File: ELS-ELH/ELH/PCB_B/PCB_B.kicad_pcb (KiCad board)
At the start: 2 copper layers, 95 x 95 mm, 22 parts, among them J1 Pressure Transducer Input, J2 Conn_01x04_Pin, J3 Conn_01x20_Pin, J4 Conn_01x20_Pin, U1 GY-87

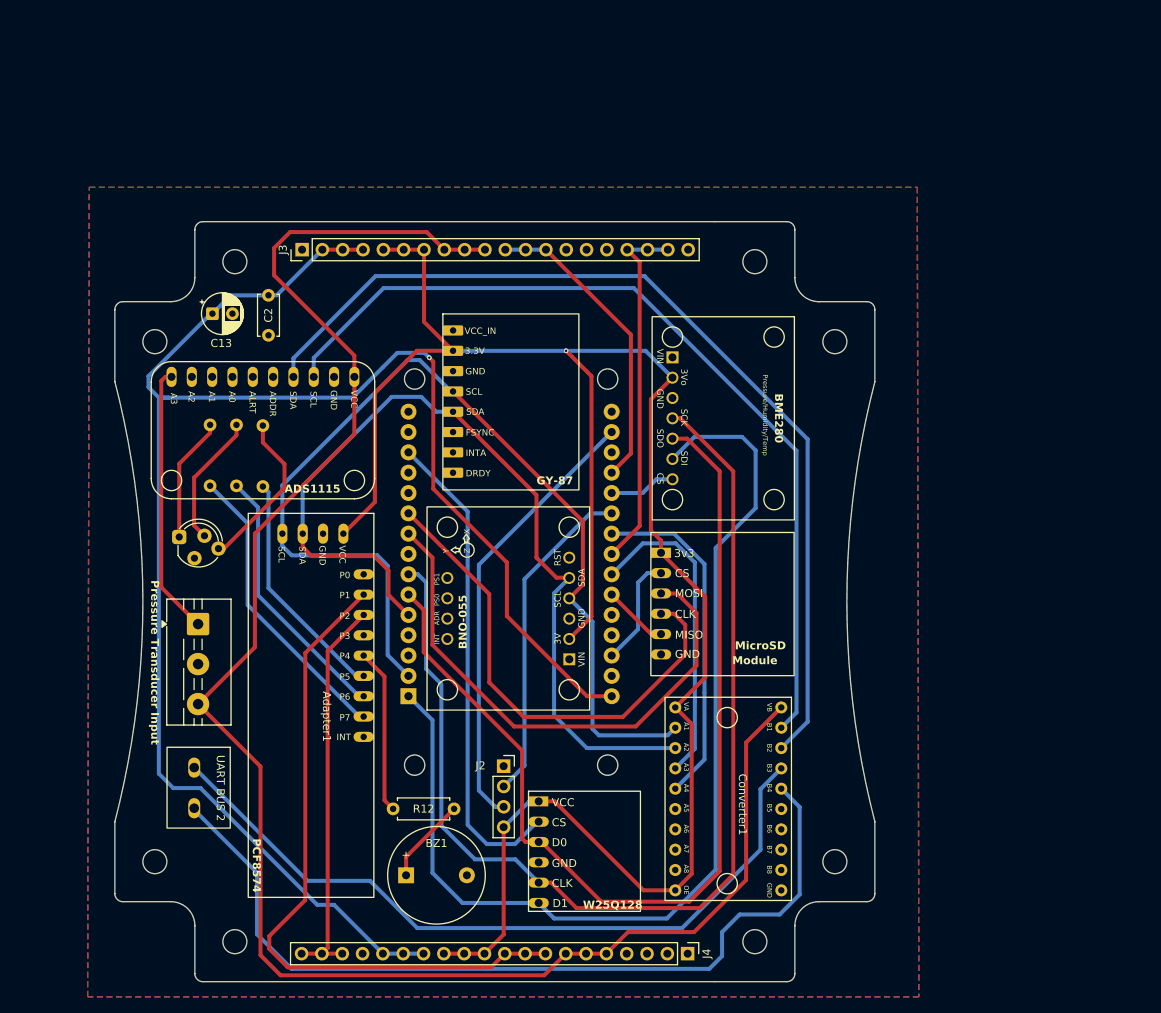
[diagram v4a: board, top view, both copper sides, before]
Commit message: General Update
Final version & manufacture files of both PCBs + codes of unit testing on modules and functionalities

* Update on net labels of both PCBs

* Update in symbols and footprints

* Unitary Tests Codes

* Update on schematics B

* Update in PCB B - new layout

* Update in schematic A

* PCB B Almost finishhed

* PCB B ready, PCB A layout ready

* Finish PCB B

* Solve DRC problems with B

* PCB A routed

* reorganized resistances

* regulator's names changed

* Update almost finished

* Finished the manufacture

---------

Co-authored-by: sofiamelo02 <sofia.melo@udea.edu.co>
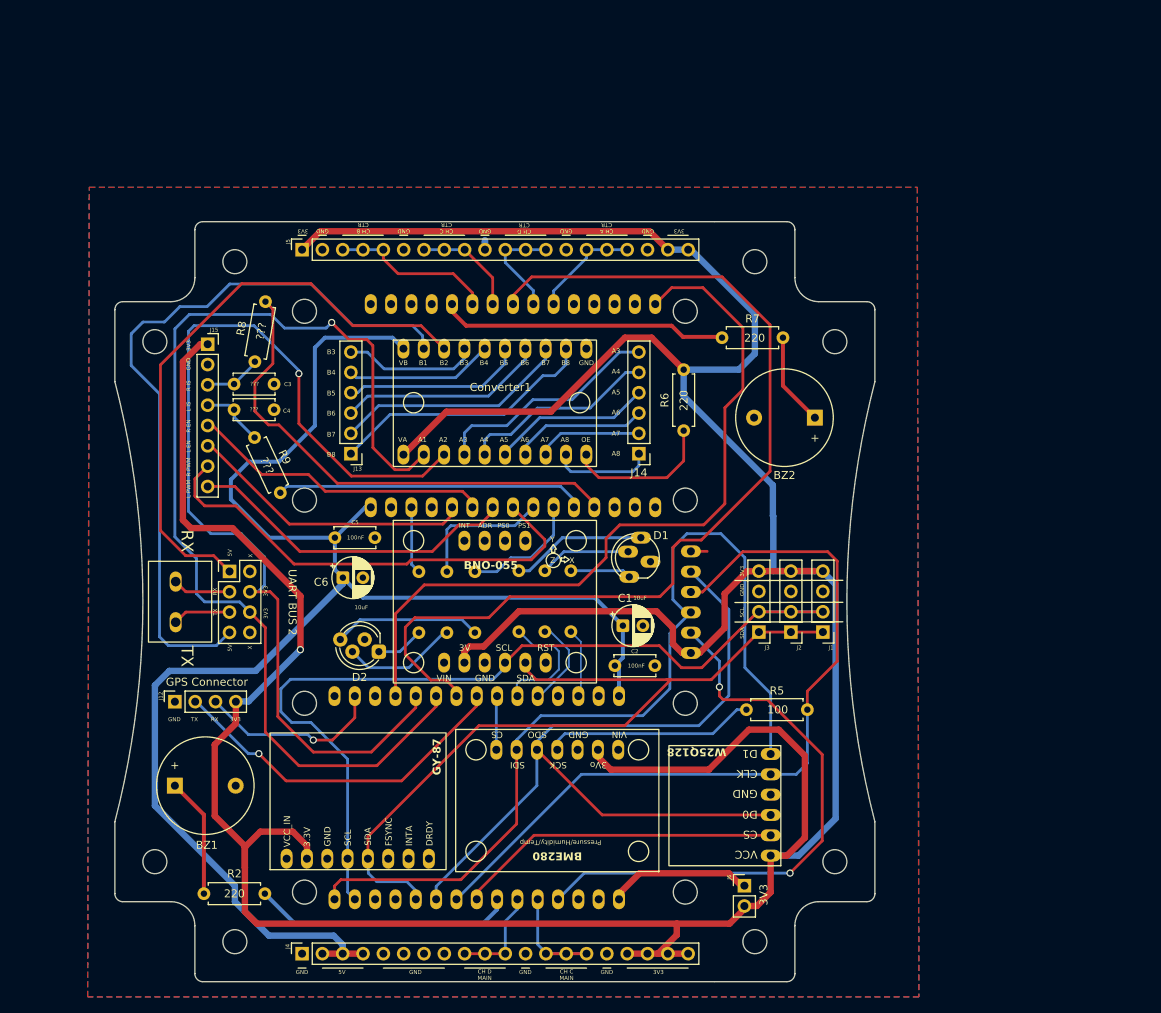
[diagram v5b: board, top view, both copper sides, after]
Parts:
- removed ADC1: ADS1115, ELH_Library:ADS1115
- removed Adapter1: PCF8574, ELH_Library:PCF8574
- removed BME2: BME280, ELH_Library:BME280
- removed Bornera7: UART BUS 2, ELH_Library:Bornera 2P
- removed C13: 10uF, Capacitor_THT:CP_Radial_D5.0mm_P2.50mm
- removed D10: LED_RKGB, ELH_Library:LED RGB
- removed ESP1: ESP32 DEVKIT V1, ELH_Library:ESP32 DEVKIT V1
- removed IMU3: BNO055, ELH_Library:BNO055
- added BME1: BME280, ELH_Library:BME280, F.Cu at (20.5, 33.8)
- added BZ2: Buzzer, Buzzer_Beeper:Buzzer_12x9.5RM7.6, F.Cu at (40.0, -23.0)
- added Bornera1: UART BUS 2, ELH_Library:Bornera 2P, F.Cu at (-35.4, -5.05)
- added C1: 10uF, Capacitor_THT:CP_Radial_D5.0mm_P2.50mm, F.Cu at (16.0, 3.00)
- added C3: ???, Capacitor_THT:C_Disc_D5.0mm_W2.5mm_P5.00mm, F.Cu at (-27.6, -27.2)
- added C4: ???, Capacitor_THT:C_Disc_D5.0mm_W2.5mm_P5.00mm, F.Cu at (-32.6, -24.0)
- added C5: 100nF, Capacitor_THT:C_Disc_D5.0mm_W2.5mm_P5.00mm, F.Cu at (-15.0, -8.00)
- added C6: 10uF, Capacitor_THT:CP_Radial_D5.0mm_P2.50mm, F.Cu at (-19.0, -3.00)
- added D1: LED_RKGB, ELH_Library:LED RGB, F.Cu at (17.1, -5.00)
- added D2: LED_RKGB, LED_THT:LED_D5.0mm-4_RGB_Staggered_Pins, F.Cu at (-14.5, 6.25)
- added ESP_CTR1: ESP32 DEVKIT V1, ELH_Library:ESP32 DEVKIT V1, B.Cu at (0.00, -25.0)
- added ESP_MAIN1: ESP32 DEVKIT V1, ELH_Library:ESP32 DEVKIT V1, B.Cu at (0.00, 25.0)
- added G***: LOGO, ELH_Library:deltav_logo, B.Cu at (32.9, -18.5)
- added G***: LOGO, ELH_Library:IREC, B.Cu at (35.8, -13.0)
- added G***: LOGO, ELH_Library:volta_logo, B.Cu at (38.4, -18.6)
- added IMU1: BNO055, ELH_Library:BNO055, F.Cu at (-12.7, -10.2)
- added J12: GPS Connector, Connector_PinSocket_2.54mm:PinSocket_1x04_P2.54mm_Vertical, F.Cu at (-40.0, 12.5)
- added J13: Conn_01x06_Pin, Connector_PinHeader_2.54mm:PinHeader_1x06_P2.54mm_Vertical, F.Cu at (-18.0, -18.5)
- added J14: Conn_01x06_Pin, Connector_PinHeader_2.54mm:PinHeader_1x06_P2.54mm_Vertical, F.Cu at (18.0, -18.5)
- added J15: Conn_01x08_Pin, Connector_PinSocket_2.54mm:PinSocket_1x08_P2.54mm_Vertical, F.Cu at (-35.9, -32.2)
- added J16: Conn_02x04_Odd_Even, Connector_PinHeader_2.54mm:PinHeader_2x04_P2.54mm_Vertical, F.Cu at (-33.2, -3.78)
- added J5: Conn_01x20_Pin, Connector_PinSocket_2.54mm:PinSocket_1x20_P2.54mm_Vertical, F.Cu at (-24.1, -44.0)
- added J6: Conn_01x02_Pin, Connector_PinHeader_2.54mm:PinHeader_1x02_P2.54mm_Vertical, F.Cu at (31.2, 35.5)
- added R1: 330, Resistor_THT:R_Axial_DIN0207_L6.3mm_D2.5mm_P7.62mm_Horizontal, B.Cu at (3.00, -3.87)
- added R10: 330, Resistor_THT:R_Axial_DIN0207_L6.3mm_D2.5mm_P7.62mm_Horizontal, B.Cu at (-2.50, 3.87)
- added R11: 330, Resistor_THT:R_Axial_DIN0207_L6.3mm_D2.5mm_P7.62mm_Horizontal, B.Cu at (-6.00, 3.87)
- added R2: 220, Resistor_THT:R_Axial_DIN0207_L6.3mm_D2.5mm_P7.62mm_Horizontal, F.Cu at (-28.8, 36.5)
- added R3: 330, Resistor_THT:R_Axial_DIN0207_L6.3mm_D2.5mm_P7.62mm_Horizontal, B.Cu at (6.25, -3.87)
- added R6: 220, Resistor_THT:R_Axial_DIN0207_L6.3mm_D2.5mm_P7.62mm_Horizontal, F.Cu at (23.6, -29.0)
- added R8: ???, Resistor_THT:R_Axial_DIN0207_L6.3mm_D2.5mm_P7.62mm_Horizontal, F.Cu at (-30.0, -30.0)
- added R9: ???, Resistor_THT:R_Axial_DIN0207_L6.3mm_D2.5mm_P7.62mm_Horizontal, F.Cu at (-30.0, -20.5)
- J1: value Pressure Transducer Input -> I2C Bus Connector 1; footprint ELH_Library:Bornera 3P -> Connector_PinHeader_2.54mm:PinHeader_1x04_P2.54mm_Vertical
- J2: value Conn_01x04_Pin -> I2C Bus Connector 2; footprint Connector_PinSocket_2.54mm:PinSocket_1x04_P2.54mm_Vertical -> Connector_PinHeader_2.54mm:PinHeader_1x04_P2.54mm_Vertical
- J3: value Conn_01x20_Pin -> I2C Bus Connector 3; footprint Connector_PinHeader_2.54mm:PinHeader_1x20_P2.54mm_Vertical -> Connector_PinHeader_2.54mm:PinHeader_1x04_P2.54mm_Vertical
- J4: footprint Connector_PinHeader_2.54mm:PinHeader_1x20_P2.54mm_Vertical -> Connector_PinSocket_2.54mm:PinSocket_1x20_P2.54mm_Vertical
- R12: value 220 -> 330; moved to B.Cu
- R5: value 330 -> 100; moved to F.Cu
- R7: value 330 -> 220; moved to F.Cu
- SD_Adapter1: moved to B.Cu
- moved R5 79.7 mm to (39.1, 13.5), turned to 180 degrees
- moved J1 77.7 mm to (41.0, 3.80), turned to 180 degrees
- moved J3 74.5 mm to (33.0, 3.80), turned to 180 degrees
- moved U1 72.7 mm to (-28.1, 33.4), turned to 90 degrees
- moved Converter1 67.0 mm to (-12.7, -32.9), turned to 0 degrees
- moved C2 63.5 mm to (20.0, 8.00), turned to 180 degrees
- moved R7 58.4 mm to (28.4, -33.0), turned to 0 degrees
- moved R4 48.6 mm to (9.50, -3.87)
- moved J4 48.2 mm to (-24.1, 44.0), turned to 90 degrees
- moved J2 39.6 mm to (37.0, 3.80), turned to 180 degrees
- moved W25QXX1 32.9 mm to (35.7, 33.0), turned to 180 degrees
- moved BZ1 31.0 mm to (-40.0, 23.0)
- moved R12 22.3 mm to (-9.50, 3.87), turned to 90 degrees
- moved SD_Adapter1 18.0 mm to (23.2, 8.95)
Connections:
- C2 pad 2: +5VA -> +5V_MCU
- Converter1 pad 1: +5V -> +5V_MCU
- Converter1 pad 11: +3.3V -> +3.3V_SENSORS
- Converter1 pad 12: /I2C1_SCL -> /TX_UART_BUS2_ESP_MAIN_3V3
- Converter1 pad 13: /I2C1_SDA -> /RX_UART_BUS2_ESP_MAIN_3V3
- Converter1 pad 14: /UART2_TX_2 -> Net-(Converter1-A3)
- Converter1 pad 15: /UART2_RX_2 -> Net-(Converter1-A4)
- Converter1 pad 16: unconnected-(Converter1-A5-Pad16) -> Net-(Converter1-A5)
- Converter1 pad 17: unconnected-(Converter1-A6-Pad17) -> Net-(Converter1-A6)
- Converter1 pad 18: unconnected-(Converter1-A7-Pad18) -> Net-(Converter1-A7)
- Converter1 pad 19: unconnected-(Converter1-A8-Pad19) -> Net-(Converter1-A8)
- Converter1 pad 2: /I2C1_SCL_1 -> /TX_UART_BUS2_5V
- Converter1 pad 20: +3.3V -> Net-(Converter1-OE)
- Converter1 pad 3: /I2C1_SDA_1 -> /RX_UART_BUS2_5V
- Converter1 pad 4: /UART2_TX_1 -> Net-(Converter1-B3)
- Converter1 pad 5: /UART2_RX_1 -> Net-(Converter1-B4)
- Converter1 pad 6: unconnected-(Converter1-B5-Pad6) -> Net-(Converter1-B5)
- Converter1 pad 7: unconnected-(Converter1-B6-Pad7) -> Net-(Converter1-B6)
- Converter1 pad 8: unconnected-(Converter1-B7-Pad8) -> Net-(Converter1-B7)
- Converter1 pad 9: unconnected-(Converter1-B8-Pad9) -> Net-(Converter1-B8)
- J1 pad 1: /PT_ADC1 -> /SDA_I2C_BUS1_ESP_MAIN_3V3
- J1 pad 2: GND -> /SCL_I2C_BUS1_ESP_MAIN_3V3
- J1 pad 3: +5V -> GND
- J2 pad 1: GND -> /SDA_I2C_BUS1_ESP_MAIN_3V3
- J2 pad 2: /UART3_TX -> /SCL_I2C_BUS1_ESP_MAIN_3V3
- J2 pad 3: /UART3_RX -> GND
- J2 pad 4: +3.3V -> +3.3V_SENSORS
- J3 pad 1: unconnected-(J3-Pin_1-Pad1) -> /SDA_I2C_BUS1_ESP_MAIN_3V3
- J3 pad 2: +5VA -> /SCL_I2C_BUS1_ESP_MAIN_3V3
- J3 pad 3: +5VA -> GND
- J3 pad 4: +5VA -> +3.3V_SENSORS
- J4 pad 1: unconnected-(J4-Pin_1-Pad1) -> GND
- J4 pad 10: /MOS1_2 -> /CH_D_MOSFET_ESP_MAIN_3V3
- J4 pad 11: +3.3V -> /CH_D_MOSFET_ESP_MAIN_3V3
- J4 pad 12: +3.3V -> GND
- J4 pad 13: +3.3V -> /CH_C_MOSFET_ESP_MAIN_3V3
- J4 pad 14: +5VA -> /CH_C_MOSFET_ESP_MAIN_3V3
- J4 pad 15: +5VA -> /CH_C_MOSFET_ESP_MAIN_3V3
- J4 pad 16: +5VA -> GND
- J4 pad 17: GND -> +3.3V_SENSORS
- J4 pad 18: /MOS2_2 -> +3.3V_SENSORS
- J4 pad 19: /MOS2_2 -> +3.3V_SENSORS
- J4 pad 2: GND -> +5V_MCU
- J4 pad 20: /MOS2_2 -> +3.3V_SENSORS
- J4 pad 3: GND -> +5V_MCU
- J4 pad 4: GND -> +5V_MCU
- J4 pad 5: +5V -> GND
- J4 pad 6: +5V -> GND
- J4 pad 7: +5V -> GND
- J4 pad 8: /MOS1_2 -> GND
- J4 pad 9: /MOS1_2 -> /CH_D_MOSFET_ESP_MAIN_3V3
- R12 pad 1: /BUZZER1 -> Net-(D2-RA)
- R12 pad 2: Net-(BZ1-+) -> /LED_RED_SIGNAL_ESP_CTR_3V3
- R4 pad 2: /LED1 -> /LED_RED_SIGNAL_ESP_MAIN_3V3
- R5 pad 1: Net-(D10-GA) -> /SCK_SPI_BUS1_ESP_MAIN_3V3
- R5 pad 2: /LED2 -> Net-(BME1-PadSCK)
- R7 pad 1: Net-(D10-BA) -> /BUZZER_SIGNAL_ESP_CTR_3V3
- R7 pad 2: /LED3 -> Net-(BZ2-+)
- SD_Adapter1 pad 1: +3.3V -> +3.3V_SENSORS
- SD_Adapter1 pad 2: /CS_SD -> /CS_SD_ESP_MAIN_3V3
- SD_Adapter1 pad 3: /SPI2_MOSI -> /MOSI_SPI_BUS1_ESP_MAIN_3V3
- SD_Adapter1 pad 4: /SPI2_SCK -> /SCK_SPI_BUS1_ESP_MAIN_3V3
- SD_Adapter1 pad 5: /SPI2_MISO -> /MISO_SPI_BUS1_ESP_MAIN_3V3
- U1 pad 2: +3.3V -> +3.3V_SENSORS
- U1 pad 4: /I2C1_SCL -> /SCL_I2C_BUS1_ESP_MAIN_3V3
- U1 pad 5: /I2C1_SDA -> /SDA_I2C_BUS1_ESP_MAIN_3V3
- W25QXX1 pad 1: +3.3V -> +3.3V_SENSORS
- W25QXX1 pad 2: /CS_FLASH -> /CS_FLASH_ESP_MAIN_3V3
- W25QXX1 pad 3: /SPI1_MISO -> /MISO_SPI_BUS1_ESP_MAIN_3V3
- W25QXX1 pad 5: /SPI1_SCK -> /SCK_SPI_BUS1_ESP_MAIN_3V3
- W25QXX1 pad 6: /SPI1_MOSI -> /MOSI_SPI_BUS1_ESP_MAIN_3V3
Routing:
- net +3.3V_SENSORS: track 0.00 -> 488.1 mm, vias 0 -> 1
- net +3.3V: track 238.3 -> 0.00 mm, vias 1 -> 0
- net +5V: track 222.0 -> 0.00 mm
- net +5VA: track 217.2 -> 0.00 mm, vias 1 -> 0
- net +5V_MCU: track 0.00 -> 193.6 mm
- net /SPI1_SCK: track 137.1 -> 0.00 mm
- net /TX_UART_BUS2_ESP_MAIN_3V3: track 0.00 -> 133.8 mm, vias 0 -> 1
- net /SPI1_MOSI: track 130.3 -> 0.00 mm
- net /I2C1_SCL: track 128.0 -> 0.00 mm
- net /RX_UART_BUS2_ESP_MAIN_3V3: track 0.00 -> 126.6 mm, vias 0 -> 1
- net /TX_UART_BUS1_ESP_MAIN_3V3: track 0.00 -> 123.6 mm
- net /SPI1_MISO: track 123.5 -> 0.00 mm
- net /I2C1_SDA_1: track 119.3 -> 0.00 mm
- net /MOSI_SPI_BUS1_ESP_MAIN_3V3: track 0.00 -> 116.8 mm
- net /SCL_I2C_BUS1_ESP_MAIN_3V3: track 0.00 -> 113.9 mm
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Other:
- board text added: "3V3"
- board text added: "5V"
- board text added: "A3"
- board text added: "A4"
- board text added: "A5"
- board text added: "A6"
- board text added: "A7"
- board text added: "A8"
- board text added: "B3"
- board text added: "B4"
- board text added: "B5"
- board text added: "B6"
- board text added: "B7"
- board text added: "B8"
- board text added: "CH A CTR"
- board text added: "CH B CTR"
- board text added: "CH C CTR"
- board text added: "CH C MAIN"
- board text added: "CH D CTR"
- board text added: "CH D MAIN"
- board text added: "GND"
- board text added: "L EN"
- board text added: "L IS"
- board text added: "L PWM"
- board text added: "R EN"
- board text added: "R IS"
- board text added: "R PWM"
- board text added: "RX"
- board text added: "SCL"
- board text added: "SDA"
- board text added: "TX"
- board text added: "X"
- board text removed: "D1"
